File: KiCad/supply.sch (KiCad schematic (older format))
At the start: 59 parts, among them IC12 74HC00PW, IC13 SN74LVC1G126DCKR, IC4 TPS7A0518PDBVT, J12 533980471, T3 BSS138APW, U1 LM62440-Q1, U2 LM62440-Q1, U3 TXB0101DBVT

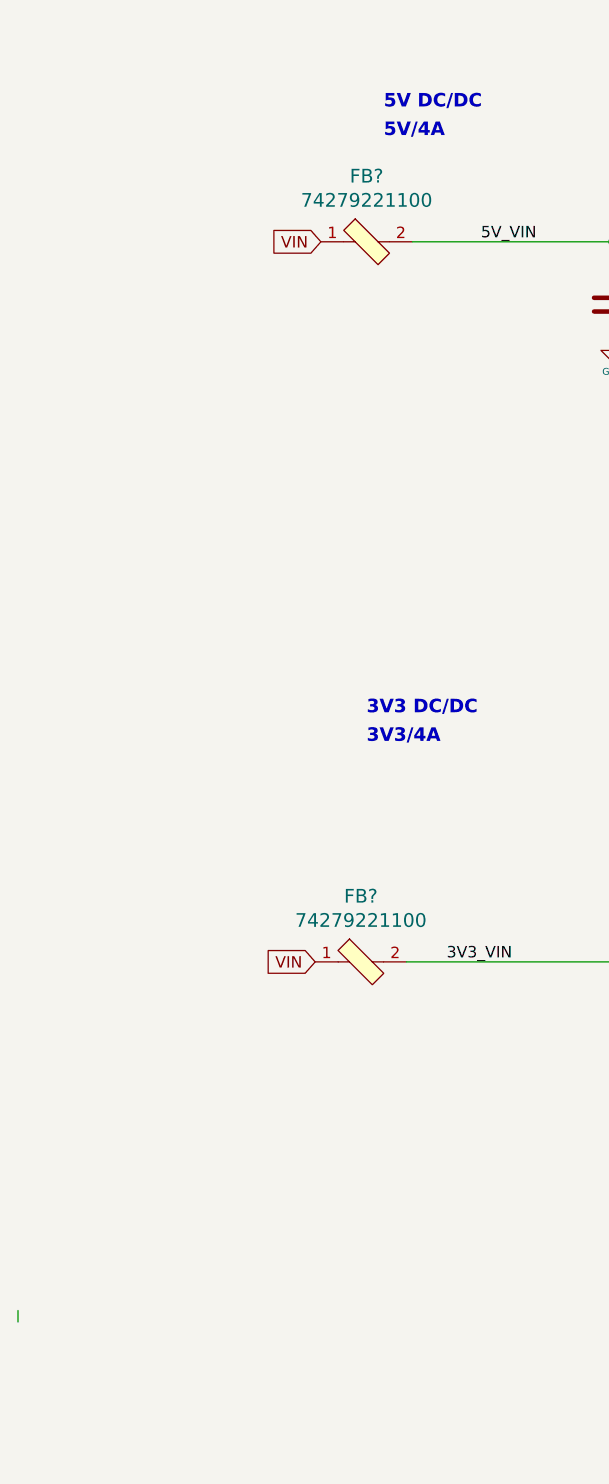
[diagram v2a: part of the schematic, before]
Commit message: Annotate parts
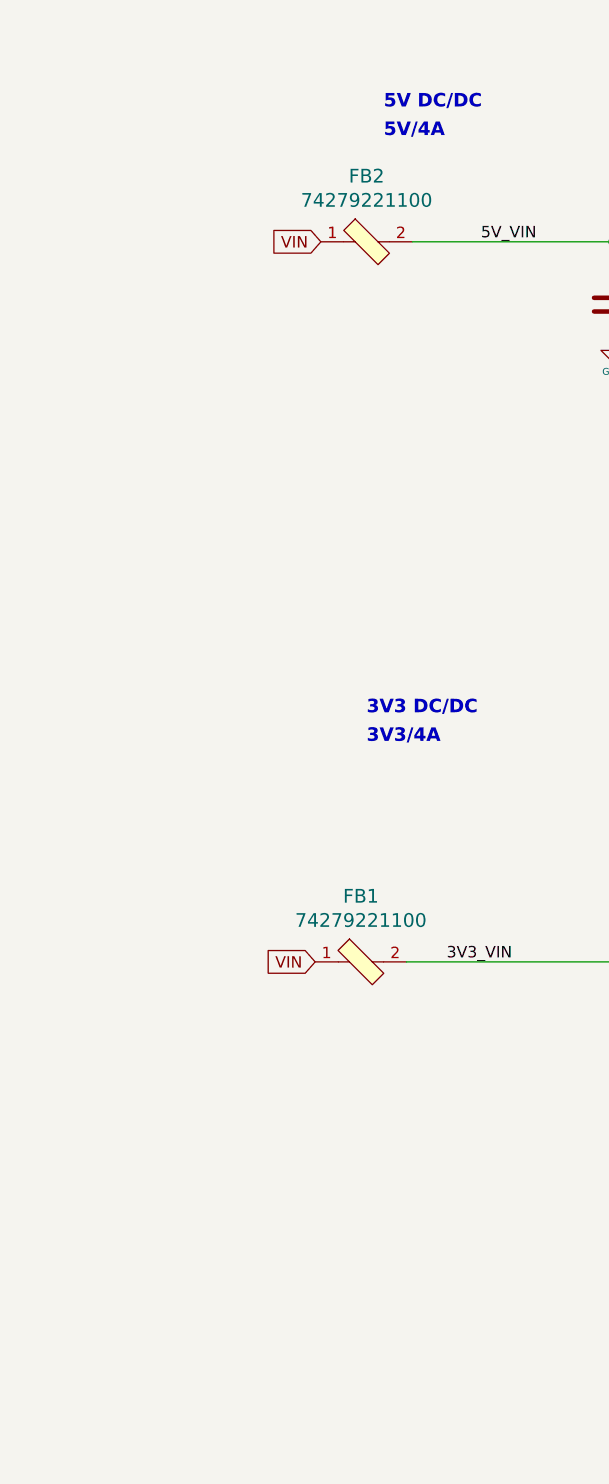
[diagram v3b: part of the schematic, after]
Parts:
- gave numbers to parts that had none: 2
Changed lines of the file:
@@
 	3250 3150 3250 3350
-Wire Wire Line
-	-275 6825 -275 6775
 Wire Wire Line
 	3600 5350 3600 5250
@@
 Connection ~ 9225 9025
 $Comp
-L antmicroFerriteBeadsandChips:74279221100 FB?
+L antmicroFerriteBeadsandChips:74279221100 FB2
 U 1 1 624FA3DC
 P 1250 2100
-F 0 "FB?" H 1250 2387 60  0000 C CNN
+F 0 "FB2" H 1250 2387 60  0000 C CNN
 F 1 "74279221100" H 1250 2281 60  0000 C CNN
 F 2 "antmicro-footprints:1206-res" H 1450 2300 60  0001 L CNN
@@
 $EndComp
 $Comp
-L antmicroFerriteBeadsandChips:74279221100 FB?
+L antmicroFerriteBeadsandChips:74279221100 FB1
 U 1 1 6250F269
 P 1225 5250
-F 0 "FB?" H 1225 5537 60  0000 C CNN
+F 0 "FB1" H 1225 5537 60  0000 C CNN
 F 1 "74279221100" H 1225 5431 60  0000 C CNN
 F 2 "antmicro-footprints:1206-res" H 1425 5450 60  0001 L CNN

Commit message: Loclib
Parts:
- FB1, FB2: footprint antmicro-footprints:1206-res -> jetson-nano-baseboard-footprints:1206-res; symbol antmicroFerriteBeadsandChips:74279221100 -> jetson-nano-baseboard:74279221100
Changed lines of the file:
@@
 Connection ~ 9225 9025
 $Comp
-L antmicroFerriteBeadsandChips:74279221100 FB2
+L jetson-nano-baseboard:74279221100 FB2
 U 1 1 624FA3DC
 P 1250 2100
 F 0 "FB2" H 1250 2387 60  0000 C CNN
 F 1 "74279221100" H 1250 2281 60  0000 C CNN
-F 2 "antmicro-footprints:1206-res" H 1450 2300 60  0001 L CNN
+F 2 "jetson-nano-baseboard-footprints:1206-res" H 1450 2300 60  0001 L CNN
 F 3 "https://www.we-online.com/catalog/datasheet/74279221100.pdf" H 1450 2400 60  0001 L CNN
 F 4 "74279221100" H 1450 2600 60  0001 L CNN "MPN"
@@
 $EndComp
 $Comp
-L antmicroFerriteBeadsandChips:74279221100 FB1
+L jetson-nano-baseboard:74279221100 FB1
 U 1 1 6250F269
 P 1225 5250
 F 0 "FB1" H 1225 5537 60  0000 C CNN
 F 1 "74279221100" H 1225 5431 60  0000 C CNN
-F 2 "antmicro-footprints:1206-res" H 1425 5450 60  0001 L CNN
+F 2 "jetson-nano-baseboard-footprints:1206-res" H 1425 5450 60  0001 L CNN
 F 3 "https://www.we-online.com/catalog/datasheet/74279221100.pdf" H 1425 5550 60  0001 L CNN
 F 4 "74279221100" H 1425 5750 60  0001 L CNN "MPN"
